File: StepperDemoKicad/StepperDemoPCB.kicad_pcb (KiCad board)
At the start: 2 copper layers, 169.3 x 65 mm, 37 parts, among them J1 Conn_01x05_Male, J2 Conn_01x01_Male, J3 Screw_Terminal_01x03, J4 Screw_Terminal_01x04, J5 Screw_Terminal_01x04, J6 Conn_01x06_Male, M1 Stepper_Motor_bipolar, SW1 SW_DIP_x01, U1 L297, U2 L298N

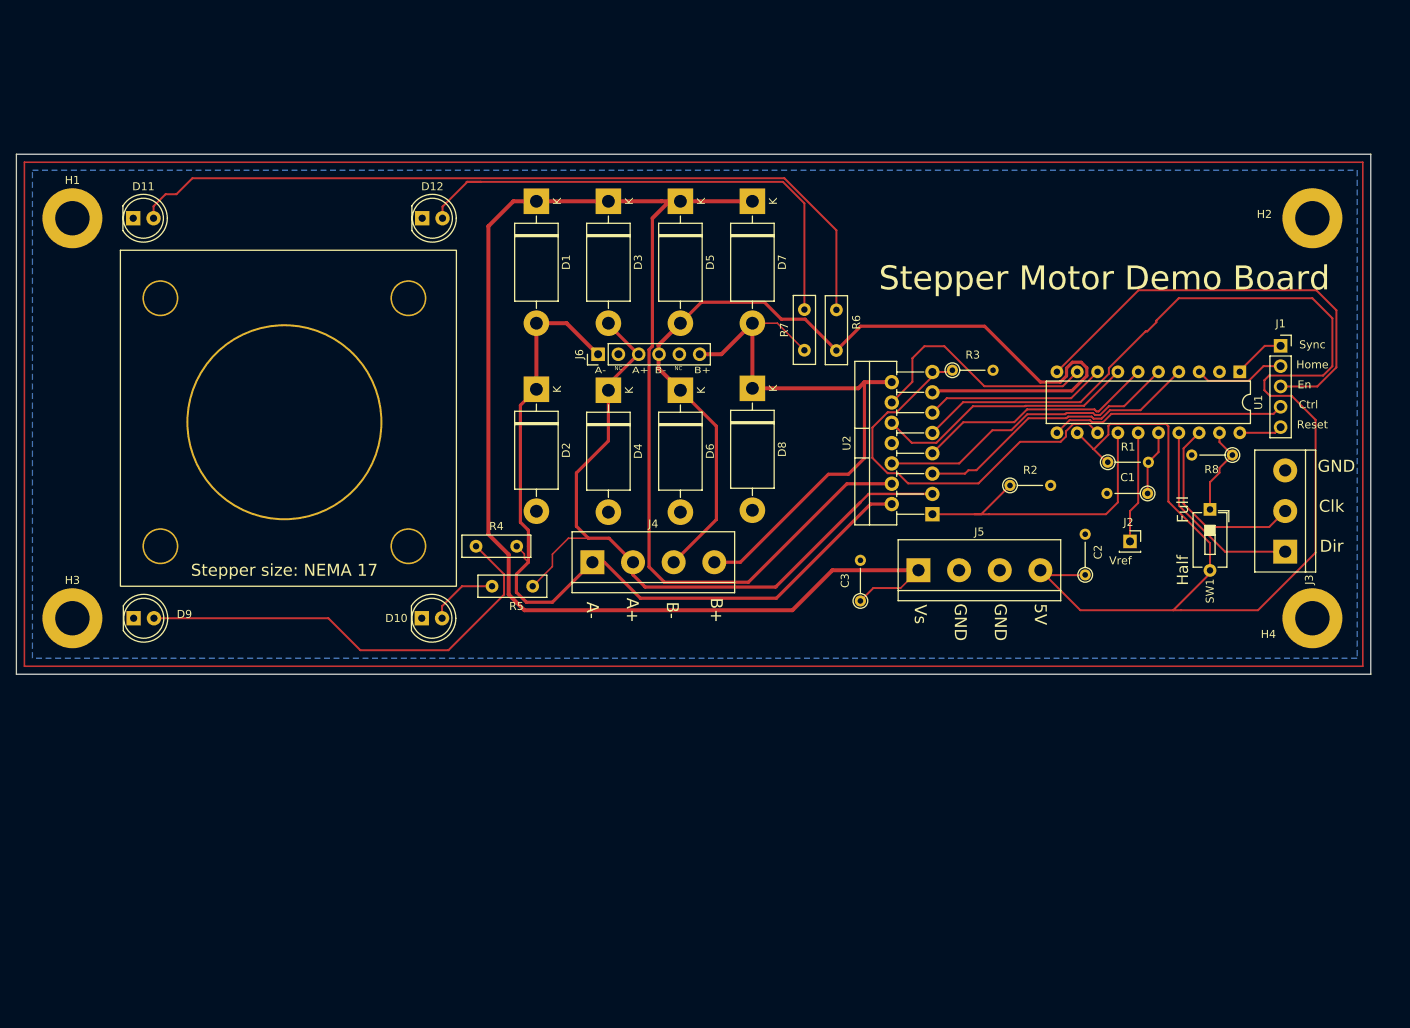
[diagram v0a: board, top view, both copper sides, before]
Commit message: Added heatsink
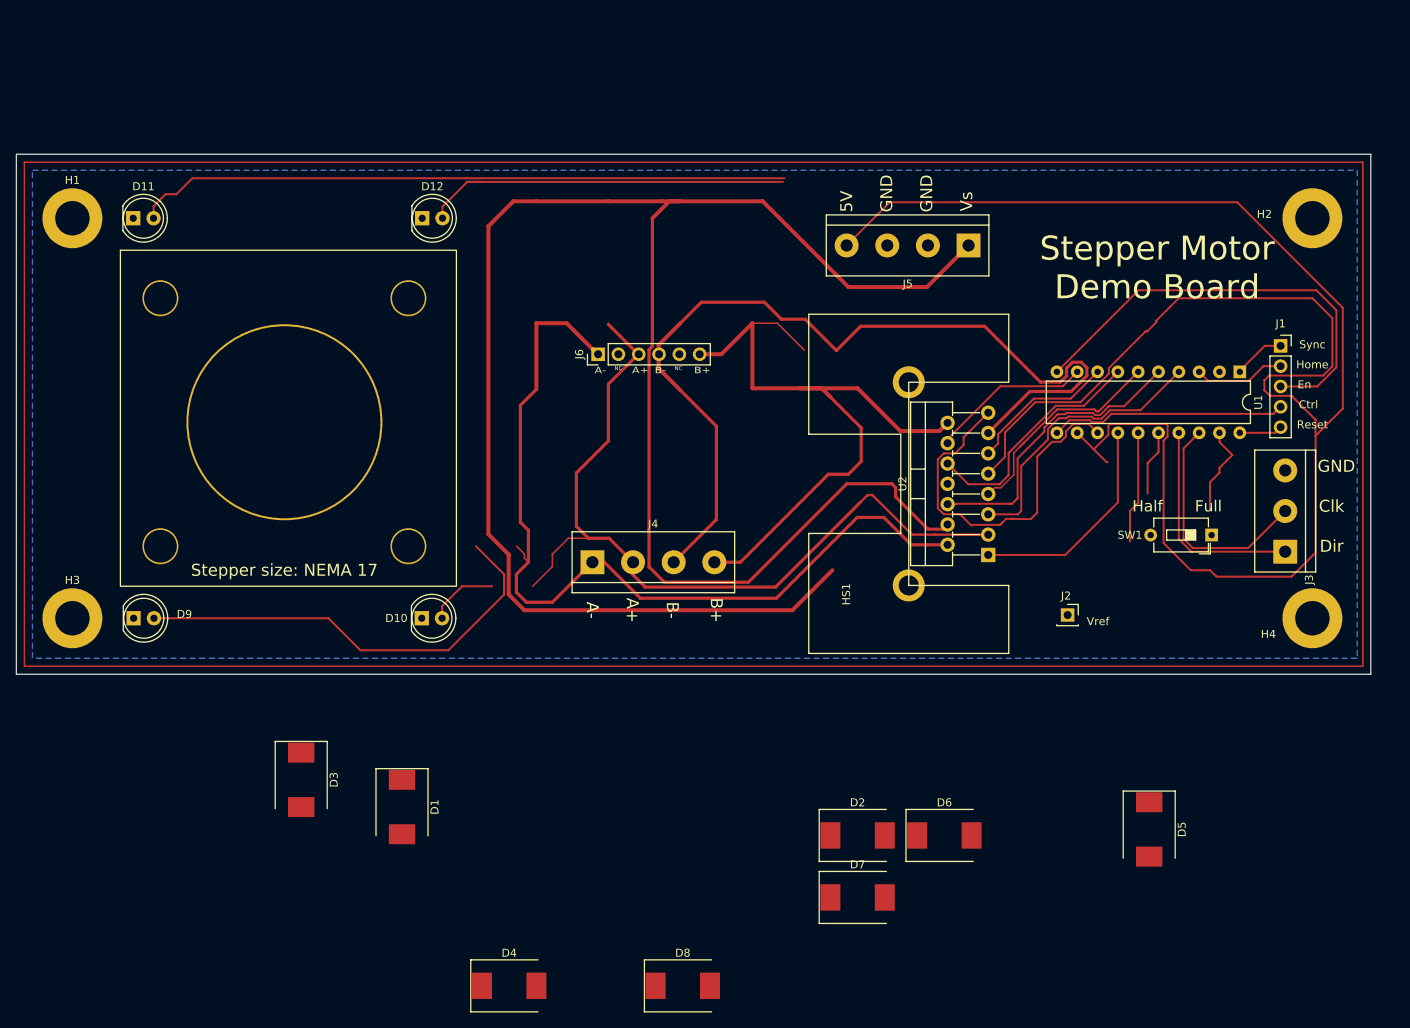
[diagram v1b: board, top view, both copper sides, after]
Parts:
- removed C1: 3.3n, Resistor_THT:R_Axial_DIN0204_L3.6mm_D1.6mm_P5.08mm_Vertical
- removed C2, C3: 100n, Resistor_THT:R_Axial_DIN0204_L3.6mm_D1.6mm_P5.08mm_Vertical
- removed R1, R8: 22k, Resistor_THT:R_Axial_DIN0204_L3.6mm_D1.6mm_P5.08mm_Vertical
- removed R2, R3: 0.5, Resistor_THT:R_Axial_DIN0204_L3.6mm_D1.6mm_P5.08mm_Vertical
- removed R4, R5, R6, R7: 2200, Resistor_THT:R_Box_L8.4mm_W2.5mm_P5.08mm
- added HS1: Heatsink_Pad, Stepper:42x25mm_multiwatt15, F.Cu at (150.0, 77.5)
- D1, D2, D3, D4, D5, D6, D7, D8: value 1N5822 -> B350; footprint Diode_THT:D_DO-201AD_P15.24mm_Horizontal -> Diode_SMD:D_SMC
- moved D5 98.0 mm to (174.6, 120.4)
- moved D7 88.0 mm to (138.2, 128.9), turned to 0 degrees
- moved D3 81.9 mm to (68.6, 114.2)
- moved D1 77.6 mm to (81.2, 117.6)
- moved D4 75.5 mm to (94.6, 139.9), turned to 0 degrees
- moved D8 75.2 mm to (116.3, 139.9), turned to 0 degrees
- moved D2 68.7 mm to (138.2, 121.2), turned to 0 degrees
- moved D6 64.7 mm to (149.0, 121.2), turned to 0 degrees
- moved J5 41.1 mm to (152.0, 47.4), turned to 180 degrees
- moved J2 12.1 mm to (164.4, 93.6)
- moved U2 8.64 mm to (154.5, 86.1)
- moved SW1 3.21 mm to (182.4, 83.6), turned to 180 degrees
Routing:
- net +5V: track 188.7 -> 237.1 mm
- net VS: track 228.7 -> 253.0 mm
- net Net-(D11-Pad2): track 101.0 -> 81.8 mm
- net Net-(D12-Pad2): track 64.2 -> 47.1 mm
- net B+: track 75.7 -> 88.8 mm
- net /SensB: track 38.4 -> 27.6 mm
- net /SigB-: track 30.6 -> 20.2 mm
- net A+: track 93.9 -> 102.8 mm
- net A-: track 103.6 -> 111.3 mm
- net B-: track 117.8 -> 112.9 mm
- net Clk: track 24.4 -> 29.2 mm
- net /Inh2: track 22.8 -> 18.6 mm
- net /SigB+: track 33.0 -> 29.8 mm
- net /SensA: track 50.5 -> 47.4 mm
- net /SigA-: track 30.2 -> 27.6 mm
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
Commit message: SMD resistors
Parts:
- moved D5 92.0 mm to (116.6, 49.0)
- moved D7 80.4 mm to (127.2, 49.2), turned to -90 degrees
- moved D3 75.0 mm to (105.8, 49.0)
- moved D8 74.9 mm to (127.0, 65.8), turned to -90 degrees
- moved D4 74.8 mm to (105.8, 66.0), turned to -90 degrees
- moved D1 69.8 mm to (95.2, 49.2)
- moved D2 69.7 mm to (95.2, 66.2), turned to -90 degrees
- moved D6 64.1 mm to (116.6, 65.8), turned to -90 degrees
- moved J6 16.6 mm to (105.8, 77.6)
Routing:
- net B-: track 112.9 -> 93.6 mm
- net A+: track 102.8 -> 95.2 mm
- net A-: track 111.3 -> 107.9 mm
- net VS: track 253.0 -> 256.2 mm
- net B+: track 88.8 -> 88.0 mm

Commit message: Update
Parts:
- added C1: 3.3n, Capacitor_SMD:C_0805_2012Metric_Pad1.18x1.45mm_HandSolder, F.Cu at (87.5, 27.9)
- added C2: 100n, Capacitor_SMD:C_0805_2012Metric_Pad1.18x1.45mm_HandSolder, F.Cu at (95.6, 21.6)
- added C3: 100n, Capacitor_SMD:C_0805_2012Metric_Pad1.18x1.45mm_HandSolder, F.Cu at (95.6, 24.6)
- added R1: 22k, Resistor_SMD:R_0805_2012Metric_Pad1.20x1.40mm_HandSolder, F.Cu at (100.4, 24.5)
- added R2: 0.5, Resistor_THT:R_Axial_DIN0204_L3.6mm_D1.6mm_P5.08mm_Vertical, F.Cu at (86.7, 21.7)
- added R3: 0.5, Resistor_THT:R_Axial_DIN0204_L3.6mm_D1.6mm_P5.08mm_Vertical, F.Cu at (86.7, 24.8)
- added R4: 330, Resistor_SMD:R_0805_2012Metric_Pad1.20x1.40mm_HandSolder, F.Cu at (100.4, 21.6)
- added R5: 330, Resistor_SMD:R_0805_2012Metric_Pad1.20x1.40mm_HandSolder, F.Cu at (97.0, 30.5)
- added R6: 330, Resistor_SMD:R_0805_2012Metric_Pad1.20x1.40mm_HandSolder, F.Cu at (101.8, 27.5)
- added R7: 330, Resistor_SMD:R_0805_2012Metric_Pad1.20x1.40mm_HandSolder, F.Cu at (92.3, 27.9)
- added R8: 22k, Resistor_SMD:R_0805_2012Metric_Pad1.20x1.40mm_HandSolder, F.Cu at (97.0, 27.6)
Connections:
- net /SigA+ renamed SigA+
- net /SigA- renamed SigA-
- net /SigB+ renamed SigB+
- net /SigB- renamed SigB-
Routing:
- net VS: track 256.2 -> 150.6 mm
- net B-: track 93.6 -> 112.6 mm
- net A-: track 107.9 -> 91.0 mm
- net B+: track 88.0 -> 78.6 mm
- net A+: track 95.2 -> 90.5 mm
